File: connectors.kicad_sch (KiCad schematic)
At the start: 4 parts

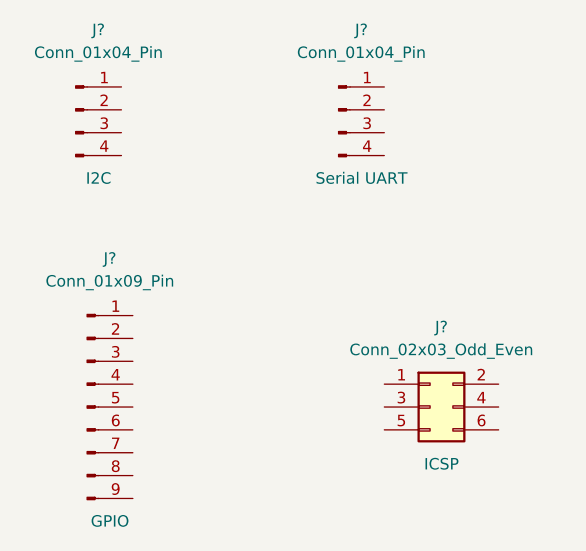
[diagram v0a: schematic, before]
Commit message: Changed locations of symbols (arrange)
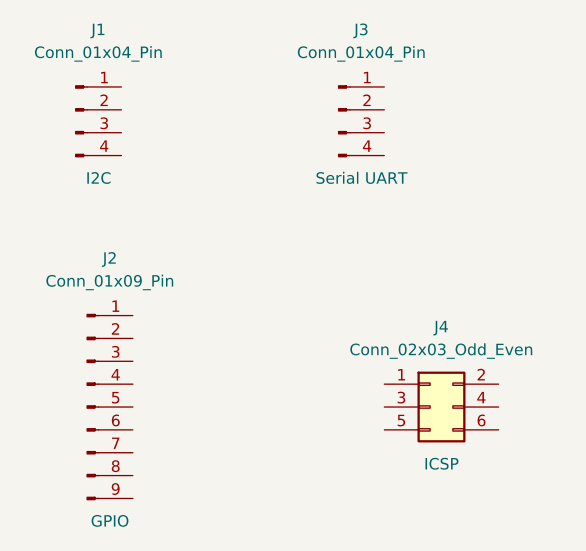
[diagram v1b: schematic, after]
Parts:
- gave numbers to parts that had none: 4
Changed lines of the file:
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@@
   (symbol (lib_id "Connector:Conn_01x09_Pin") (at 124.46 90.17 0) (unit 1)
     (in_bom yes) (on_board yes) (dnp no)
-    (property "Reference" "J?" (at 127 73.66 0)
+    (property "Reference" "J2" (at 127 73.66 0)
       (effects (font (size 1.27 1.27)))
     )
@@
       (project "MCU Datalogger"
         (path "/a2e2aee7-f3a1-41aa-a08b-33521bd80092/7aad608c-7ebf-4703-a978-c452454cad03"
-          (reference "J?") (unit 1)
+          (reference "J2") (unit 1)
         )
       )
@@
   (symbol (lib_id "Connector:Conn_01x04_Pin") (at 152.4 57.15 0) (unit 1)
     (in_bom yes) (on_board yes) (dnp no)
-    (property "Reference" "J?" (at 154.94 48.26 0)
+    (property "Reference" "J3" (at 154.94 48.26 0)
       (effects (font (size 1.27 1.27)))
     )
@@
       (project "MCU Datalogger"
         (path "/a2e2aee7-f3a1-41aa-a08b-33521bd80092/7aad608c-7ebf-4703-a978-c452454cad03"
-          (reference "J?") (unit 1)
+          (reference "J3") (unit 1)
         )
       )
@@
   (symbol (lib_id "Connector:Conn_01x04_Pin") (at 123.19 57.15 0) (unit 1)
     (in_bom yes) (on_board yes) (dnp no)
-    (property "Reference" "J?" (at 125.73 48.26 0)
+    (property "Reference" "J1" (at 125.73 48.26 0)
       (effects (font (size 1.27 1.27)))
     )
@@
       (project "MCU Datalogger"
         (path "/a2e2aee7-f3a1-41aa-a08b-33521bd80092/7aad608c-7ebf-4703-a978-c452454cad03"
-          (reference "J?") (unit 1)
+          (reference "J1") (unit 1)
         )
       )
@@
   (symbol (lib_id "Connector_Generic:Conn_02x03_Odd_Even") (at 162.56 90.17 0) (unit 1)
     (in_bom yes) (on_board yes) (dnp no)
-    (property "Reference" "J?" (at 163.83 81.28 0)
+    (property "Reference" "J4" (at 163.83 81.28 0)
       (effects (font (size 1.27 1.27)))
     )
@@
       (project "MCU Datalogger"
         (path "/a2e2aee7-f3a1-41aa-a08b-33521bd80092/7aad608c-7ebf-4703-a978-c452454cad03"
-          (reference "J?") (unit 1)
+          (reference "J4") (unit 1)
         )
       )

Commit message: Completed symbol-footprint associations
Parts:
- J1, J3: footprint (none) -> Connector_PinHeader_2.54mm:PinHeader_1x04_P2.54mm_Vertical
- J2: footprint (none) -> Connector_PinHeader_2.54mm:PinHeader_1x09_P2.54mm_Vertical
- J4: footprint (none) -> Connector_PinHeader_2.54mm:PinHeader_2x03_P2.54mm_Vertical
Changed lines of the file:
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@@
       (effects (font (size 1.27 1.27)))
     )
-    (property "Footprint" "" (at 124.46 90.17 0)
+    (property "Footprint" "Connector_PinHeader_2.54mm:PinHeader_1x09_P2.54mm_Vertical" (at 124.46 90.17 0)
       (effects (font (size 1.27 1.27)) hide)
     )
@@
       (effects (font (size 1.27 1.27)))
     )
-    (property "Footprint" "" (at 152.4 57.15 0)
+    (property "Footprint" "Connector_PinHeader_2.54mm:PinHeader_1x04_P2.54mm_Vertical" (at 152.4 57.15 0)
       (effects (font (size 1.27 1.27)) hide)
     )
@@
       (effects (font (size 1.27 1.27)))
     )
-    (property "Footprint" "" (at 123.19 57.15 0)
+    (property "Footprint" "Connector_PinHeader_2.54mm:PinHeader_1x04_P2.54mm_Vertical" (at 123.19 57.15 0)
       (effects (font (size 1.27 1.27)) hide)
     )
@@
       (effects (font (size 1.27 1.27)))
     )
-    (property "Footprint" "" (at 162.56 90.17 0)
+    (property "Footprint" "Connector_PinHeader_2.54mm:PinHeader_2x03_P2.54mm_Vertical" (at 162.56 90.17 0)
       (effects (font (size 1.27 1.27)) hide)
     )

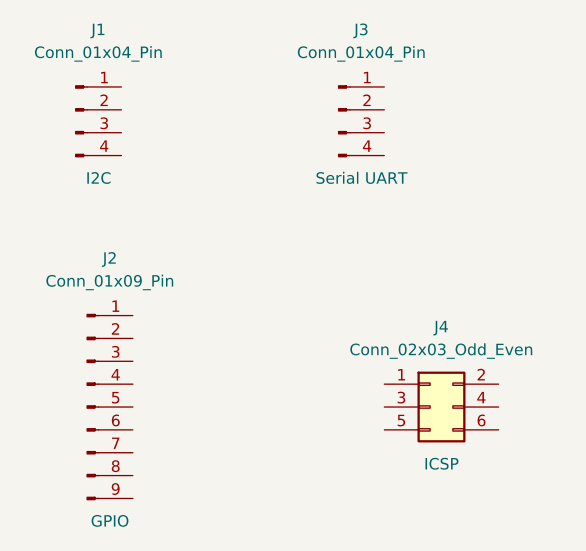
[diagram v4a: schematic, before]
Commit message: Completed wiring in the second sheet.
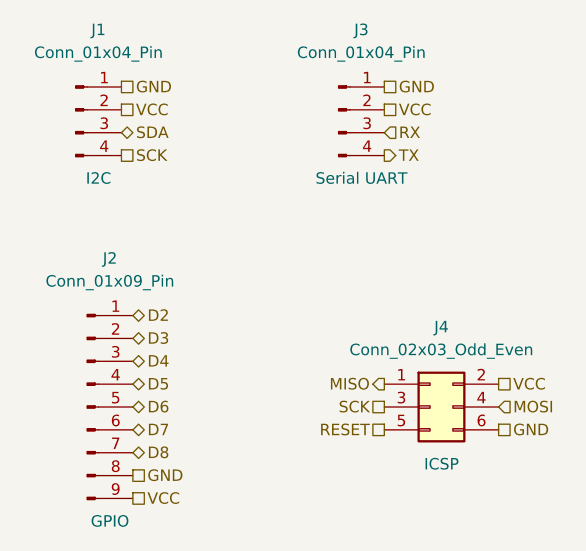
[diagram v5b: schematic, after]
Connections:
- net D2: now reaches J2.1 (Pin_1)
- net D3: now reaches J2.2 (Pin_2)
- net D4: now reaches J2.3 (Pin_3)
- net D5: now reaches J2.4 (Pin_4)
- net D6: now reaches J2.5 (Pin_5)
- net D7: now reaches J2.6 (Pin_6)
- net D8: now reaches J2.7 (Pin_7)
- net GND: now reaches J2.8 (Pin_8)
- net GND: now also J1.1 (Pin_1), J3.1 (Pin_1), J4.6 (Pin_6)
- net VCC: now reaches J2.9 (Pin_9)
- net VCC: now also J1.2 (Pin_2), J3.2 (Pin_2), J4.2 (Pin_2)
- net RX: now reaches J3.3 (Pin_3)
- net TX: now reaches J3.4 (Pin_4)
- net SDA: now reaches J1.3 (Pin_3)
- net SCK: now reaches J1.4 (Pin_4)
- net SCK: now also J4.3 (Pin_3)
- net MISO: now reaches J4.1 (Pin_1)
- net MOSI: now reaches J4.4 (Pin_4)
- net RESET: now reaches J4.5 (Pin_5)
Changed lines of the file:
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@@
 (kicad_sch (version 20230121) (generator eeschema)
   (paper "A4")
+  (hierarchical_label "D5" (shape bidirectional) (at 129.54 87.63 0) (fields_autoplaced)
+    (effects (font (size 1.27 1.27)) (justify left))
+  )
+  (hierarchical_label "VCC" (shape passive) (at 129.54 100.33 0) (fields_autoplaced)
+    (effects (font (size 1.27 1.27)) (justify left))
+  )
+  (hierarchical_label "VCC" (shape passive) (at 157.48 57.15 0) (fields_autoplaced)
+    (effects (font (size 1.27 1.27)) (justify left))
+  )
+  (hierarchical_label "VCC" (shape passive) (at 128.27 57.15 0) (fields_autoplaced)
+    (effects (font (size 1.27 1.27)) (justify left))
+  )
+  (hierarchical_label "D4" (shape bidirectional) (at 129.54 85.09 0) (fields_autoplaced)
+    (effects (font (size 1.27 1.27)) (justify left))
+  )
+  (hierarchical_label "RESET" (shape passive) (at 157.48 92.71 180) (fields_autoplaced)
+    (effects (font (size 1.27 1.27)) (justify right))
+  )
+  (hierarchical_label "MOSI" (shape input) (at 170.18 90.17 0) (fields_autoplaced)
+    (effects (font (size 1.27 1.27)) (justify left))
+  )
+  (hierarchical_label "SCK" (shape passive) (at 128.27 62.23 0) (fields_autoplaced)
+    (effects (font (size 1.27 1.27)) (justify left))
+  )
+  (hierarchical_label "GND" (shape passive) (at 129.54 97.79 0) (fields_autoplaced)
+    (effects (font (size 1.27 1.27)) (justify left))
+  )
+  (hierarchical_label "TX" (shape output) (at 157.48 62.23 0) (fields_autoplaced)
+    (effects (font (size 1.27 1.27)) (justify left))
+  )
+  (hierarchical_label "D8" (shape bidirectional) (at 129.54 95.25 0) (fields_autoplaced)
+    (effects (font (size 1.27 1.27)) (justify left))
+  )
+  (hierarchical_label "RX" (shape input) (at 157.48 59.69 0) (fields_autoplaced)
+    (effects (font (size 1.27 1.27)) (justify left))
+  )
+  (hierarchical_label "D6" (shape bidirectional) (at 129.54 90.17 0) (fields_autoplaced)
+    (effects (font (size 1.27 1.27)) (justify left))
+  )
+  (hierarchical_label "MISO" (shape output) (at 157.48 87.63 180) (fields_autoplaced)
+    (effects (font (size 1.27 1.27)) (justify right))
+  )
+  (hierarchical_label "VCC" (shape passive) (at 170.18 87.63 0) (fields_autoplaced)
+    (effects (font (size 1.27 1.27)) (justify left))
+  )
+  (hierarchical_label "GND" (shape passive) (at 170.18 92.71 0) (fields_autoplaced)
+    (effects (font (size 1.27 1.27)) (justify left))
+  )
+  (hierarchical_label "D2" (shape bidirectional) (at 129.54 80.01 0) (fields_autoplaced)
+    (effects (font (size 1.27 1.27)) (justify left))
+  )
+  (hierarchical_label "D7" (shape bidirectional) (at 129.54 92.71 0) (fields_autoplaced)
+    (effects (font (size 1.27 1.27)) (justify left))
+  )
+  (hierarchical_label "GND" (shape passive) (at 128.27 54.61 0) (fields_autoplaced)
+    (effects (font (size 1.27 1.27)) (justify left))
+  )
+  (hierarchical_label "SCK" (shape passive) (at 157.48 90.17 180) (fields_autoplaced)
+    (effects (font (size 1.27 1.27)) (justify right))
+  )
+  (hierarchical_label "GND" (shape passive) (at 157.48 54.61 0) (fields_autoplaced)
+    (effects (font (size 1.27 1.27)) (justify left))
+  )
+  (hierarchical_label "SDA" (shape bidirectional) (at 128.27 59.69 0) (fields_autoplaced)
+    (effects (font (size 1.27 1.27)) (justify left))
+  )
+  (hierarchical_label "D3" (shape bidirectional) (at 129.54 82.55 0) (fields_autoplaced)
+    (effects (font (size 1.27 1.27)) (justify left))
+  )
   (symbol (lib_id "Connector:Conn_01x09_Pin") (at 124.46 90.17 0) (unit 1)
     (in_bom yes) (on_board yes) (dnp no)
